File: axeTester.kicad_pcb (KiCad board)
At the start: 4 copper layers, 56.5 x 99.8 mm, 43 parts

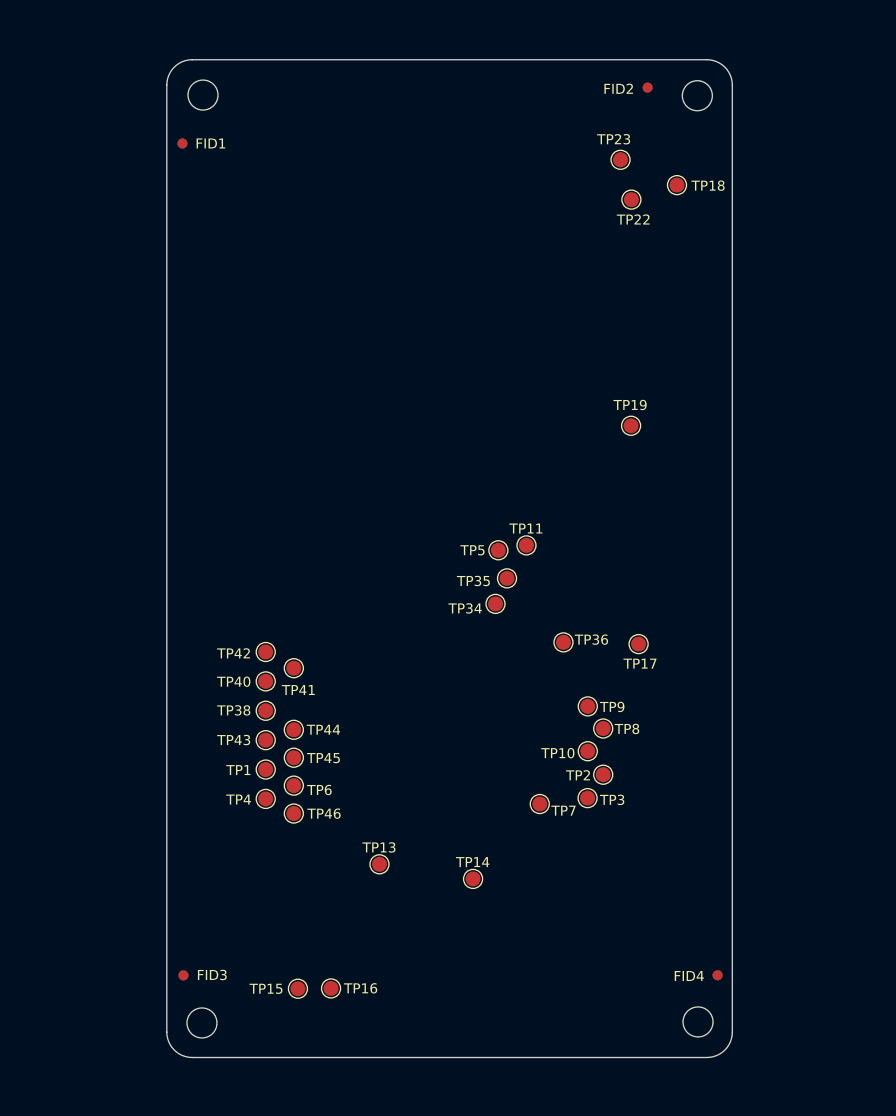
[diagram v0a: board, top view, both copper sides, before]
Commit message: switched to more common THT pogo pins. wired up connectors
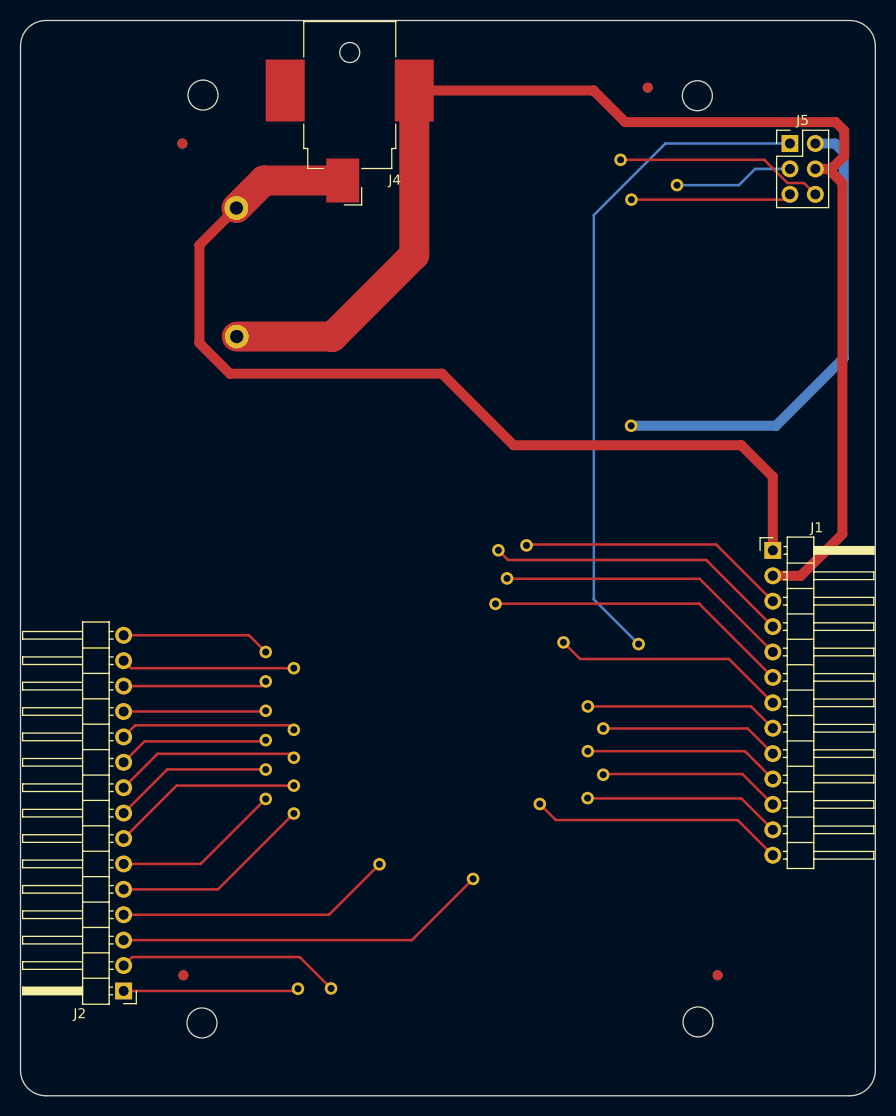
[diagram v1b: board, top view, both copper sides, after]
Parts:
- added J1: Conn_01x13, Connector_PinHeader_2.54mm:PinHeader_1x13_P2.54mm_Horizontal, F.Cu at (137.8, 96.6)
- added J2: Conn_01x15, Connector_PinHeader_2.54mm:PinHeader_1x15_P2.54mm_Horizontal, F.Cu at (72.9, 140.6)
- added J4: PJ-036AH-SMT, Connector_BarrelJack:BarrelJack_CUI_PJ-036AH-SMT_Horizontal, F.Cu at (95.5, 53.8)
- added J5: Conn_02x03_Counter_Clockwise, Connector_PinHeader_2.54mm:PinHeader_2x03_P2.54mm_Vertical, F.Cu at (139.5, 55.9)
- added TP12: P75-E2, axeTester:pogopin-P75-E2-1.3, B.Cu at (84.2, 75.2)
- added TP20: P75-E2, axeTester:pogopin-P75-E2-1.3, B.Cu at (84.2, 62.4)
- TP1, TP10, TP11, TP13, TP14, TP15, TP16, TP17, TP18, TP19, TP2, TP22, TP23, TP3, TP34, TP35, TP36, TP38, TP4, TP40, TP41, TP42, TP43, TP44, TP45, TP46, TP5, TP6, TP7, TP8, TP9: value TestPoint -> P50-E2; footprint TestPoint:TestPoint_Pad_D1.5mm -> axeTester:pogopin-P50-E2-0.68; moved to B.Cu
- turned TP1 to 180 degrees
- turned TP10 to 180 degrees
- turned TP11 to 180 degrees
- turned TP13 to 180 degrees
- turned TP14 to 180 degrees
- turned TP15 to 180 degrees
- turned TP16 to 180 degrees
- turned TP17 to 180 degrees
- turned TP18 to 180 degrees
- turned TP19 to 180 degrees
- turned TP2 to 180 degrees
- turned TP22 to 180 degrees
- turned TP23 to 180 degrees
- turned TP3 to 180 degrees
- turned TP34 to 180 degrees
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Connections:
- TP1 pad 1: unconnected-(TP1-Pad1) -> /BO
- TP10 pad 1: unconnected-(TP10-Pad1) -> /?1
- TP11 pad 1: unconnected-(TP11-Pad1) -> /RST_N
- TP13 pad 1: unconnected-(TP13-Pad1) -> /1V8
- TP14 pad 1: unconnected-(TP14-Pad1) -> /0V8
- TP15 pad 1: unconnected-(TP15-Pad1) -> /FAN_PWM
- TP16 pad 1: unconnected-(TP16-Pad1) -> /FAN_TACH
- TP17 pad 1: unconnected-(TP17-Pad1) -> /EN
- TP18 pad 1: unconnected-(TP18-Pad1) -> /P_TX
- TP19 pad 1: unconnected-(TP19-Pad1) -> /3V3
- TP2 pad 1: unconnected-(TP2-Pad1) -> /?2
- TP22 pad 1: unconnected-(TP22-Pad1) -> /P_RX
- TP23 pad 1: unconnected-(TP23-Pad1) -> /IO0
- TP3 pad 1: unconnected-(TP3-Pad1) -> /?3
- TP34 pad 1: unconnected-(TP34-Pad1) -> /VDD1_0
- TP35 pad 1: unconnected-(TP35-Pad1) -> /VDD2_0
- TP36 pad 1: unconnected-(TP36-Pad1) -> /VDD3_0
- TP38 pad 1: unconnected-(TP38-Pad1) -> /NRSTO
- TP4 pad 1: unconnected-(TP4-Pad1) -> /?5
- TP40 pad 1: unconnected-(TP40-Pad1) -> /VDD3_1
- TP41 pad 1: unconnected-(TP41-Pad1) -> /VDD2_1
- TP42 pad 1: unconnected-(TP42-Pad1) -> /VDD1_1
- TP43 pad 1: unconnected-(TP43-Pad1) -> /RI
- TP44 pad 1: unconnected-(TP44-Pad1) -> /CLKO
- TP45 pad 1: unconnected-(TP45-Pad1) -> /CO
- TP46 pad 1: unconnected-(TP46-Pad1) -> /PIN_MODE
- TP5 pad 1: unconnected-(TP5-Pad1) -> /CI
- TP6 pad 1: unconnected-(TP6-Pad1) -> /?4
- TP7 pad 1: unconnected-(TP7-Pad1) -> /CLKI
- TP8 pad 1: unconnected-(TP8-Pad1) -> /BI
- TP9 pad 1: unconnected-(TP9-Pad1) -> /RO
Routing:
- net /GND: track 0.00 -> 135.3 mm
- net /VIN: track 0.00 -> 97.0 mm
- net /EN: track 0.00 -> 67.3 mm
- net /3V3: track 0.00 -> 47.9 mm
- net /0V8: track 0.00 -> 37.5 mm
- net /VDD1_0: track 0.00 -> 30.8 mm
- net /CI: track 0.00 -> 30.6 mm
- net /VDD2_0: track 0.00 -> 29.6 mm
- net /1V8: track 0.00 -> 27.7 mm
- net /RST_N: track 0.00 -> 27.0 mm
- net /CLKI: track 0.00 -> 25.4 mm
- net /VDD3_0: track 0.00 -> 23.4 mm
- net /FAN_TACH: track 0.00 -> 22.4 mm
- net /IO0: track 0.00 -> 20.9 mm
- net /PIN_MODE: track 0.00 -> 20.2 mm
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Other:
- board size 56.5 x 99.8 mm -> 85.5 x 107.5 mm
- copper layers 4 -> 2

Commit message: removed extra files. updated readme
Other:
- board text added: "axeTester v1"
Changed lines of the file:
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@@
 		(layer "User.2")
+	)
+	(gr_text "axeTester v1"
+		(at 112.4 149.62 0)
+		(layer "B.SilkS")
+		(effects
+			(font
+				(size 1 1)
+				(thickness 0.15)
+			)
+			(justify left bottom mirror)
+		)
 	)
 	(segment
